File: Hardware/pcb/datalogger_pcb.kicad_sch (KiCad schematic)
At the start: 45 parts, among them J1 Micro_SD_Card_Det2, J2 Switch OUT, SW1 SW_Wuerth_450301014042, U1 DS3231MZ

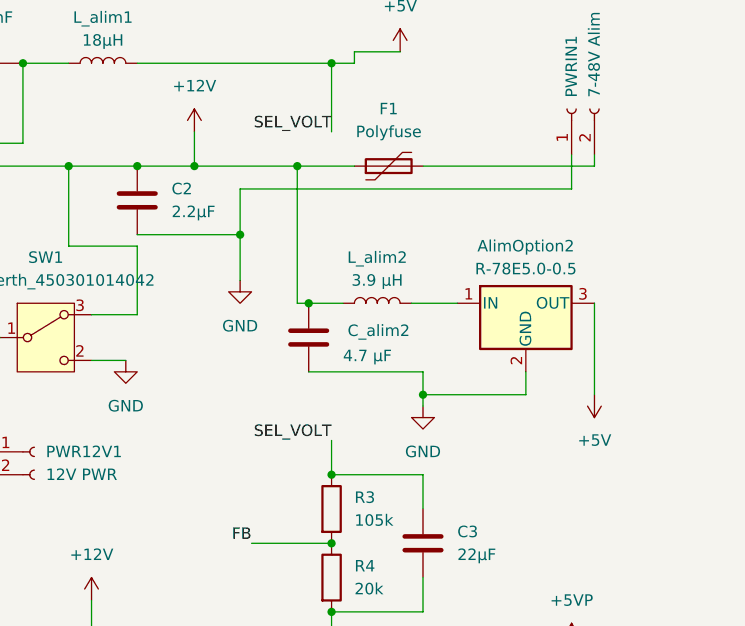
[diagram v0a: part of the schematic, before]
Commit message: Corrected screw diameter error
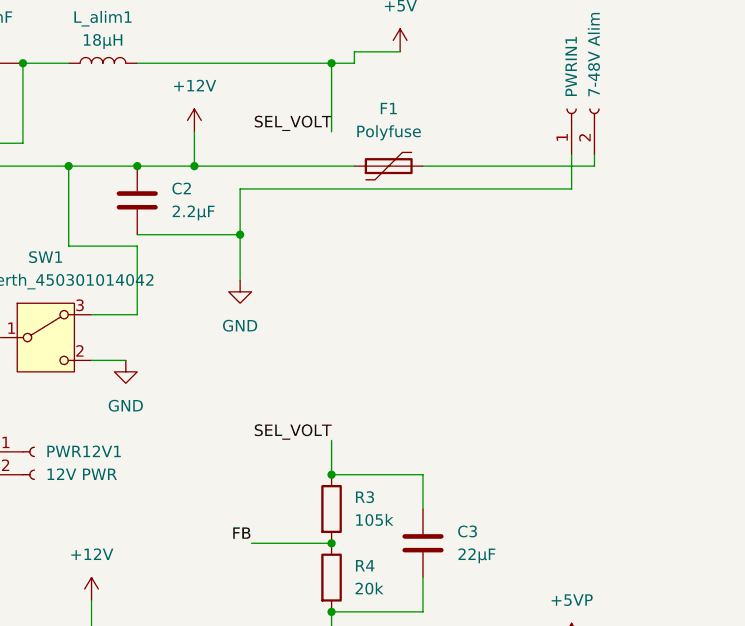
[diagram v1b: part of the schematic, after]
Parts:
- removed AlimOption2: R-78E5.0-0.5, Converter_DCDC:Converter_DCDC_RECOM_R-78E-0.5_THT, symbol Regulator_Switching:R-78E5.0-0.5
- removed C_alim2: 4.7 µF, Capacitor_SMD:C_1812_4532Metric_Pad1.57x3.40mm_HandSolder, symbol Device:C
- removed L_alim2: 3.9 µH, useful:RLS-397, symbol Device:L

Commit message: Added latching shutdown
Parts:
- removed Diodeprotectionalim1: 1N5817, Diode_THT:D_DO-41_SOD81_P10.16mm_Horizontal, symbol Diode:1N5817
- removed R6: 10k, Resistor_SMD:R_0805_2012Metric_Pad1.20x1.40mm_HandSolder, symbol Device:R
- added P_MOSFET1: Si2319CDS, Package_TO_SOT_SMD:SOT-23, symbol Transistor_FET:Si2319CDS
- added R_pullup_int1, R_pullup_shtdwn1: 100k, Resistor_SMD:R_0805_2012Metric_Pad1.20x1.40mm_HandSolder, symbol Device:R
- added U2: SN74LVC2G00DCTR, nand:SSOP-8_2.95x2.8mm_P0.65mm - SN74LVC2G00, symbol SN74LVC2G00DCTR:SN74LVC2G00DCTR
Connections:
- net +5V: now also P_MOSFET1.3 (D), R_pullup_int1.1, R_pullup_shtdwn1.2, U2.8 (VCC)
- net +5VP: now also P_MOSFET1.2 (S)
- net GND: now also U2.4 (GND)
- net at A1.20 (GPIO15), GPIO14-1.3 (Pin_3): no longer U1.3 (~{INT}/SQW)
- new net: P_MOSFET1.1 (G), U2.6 (2B), U2.7 (1Y)
- new net: U2.2 (1B), U2.3 (2Y)
- new net RTC_INT: R_pullup_int1.2, U1.3 (~{INT}/SQW), U2.1 (1A)
- new net SHTDWN_CTRL: R_pullup_shtdwn1.1, U2.5 (2A)
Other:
- moved on the sheet: 5VPOUT1

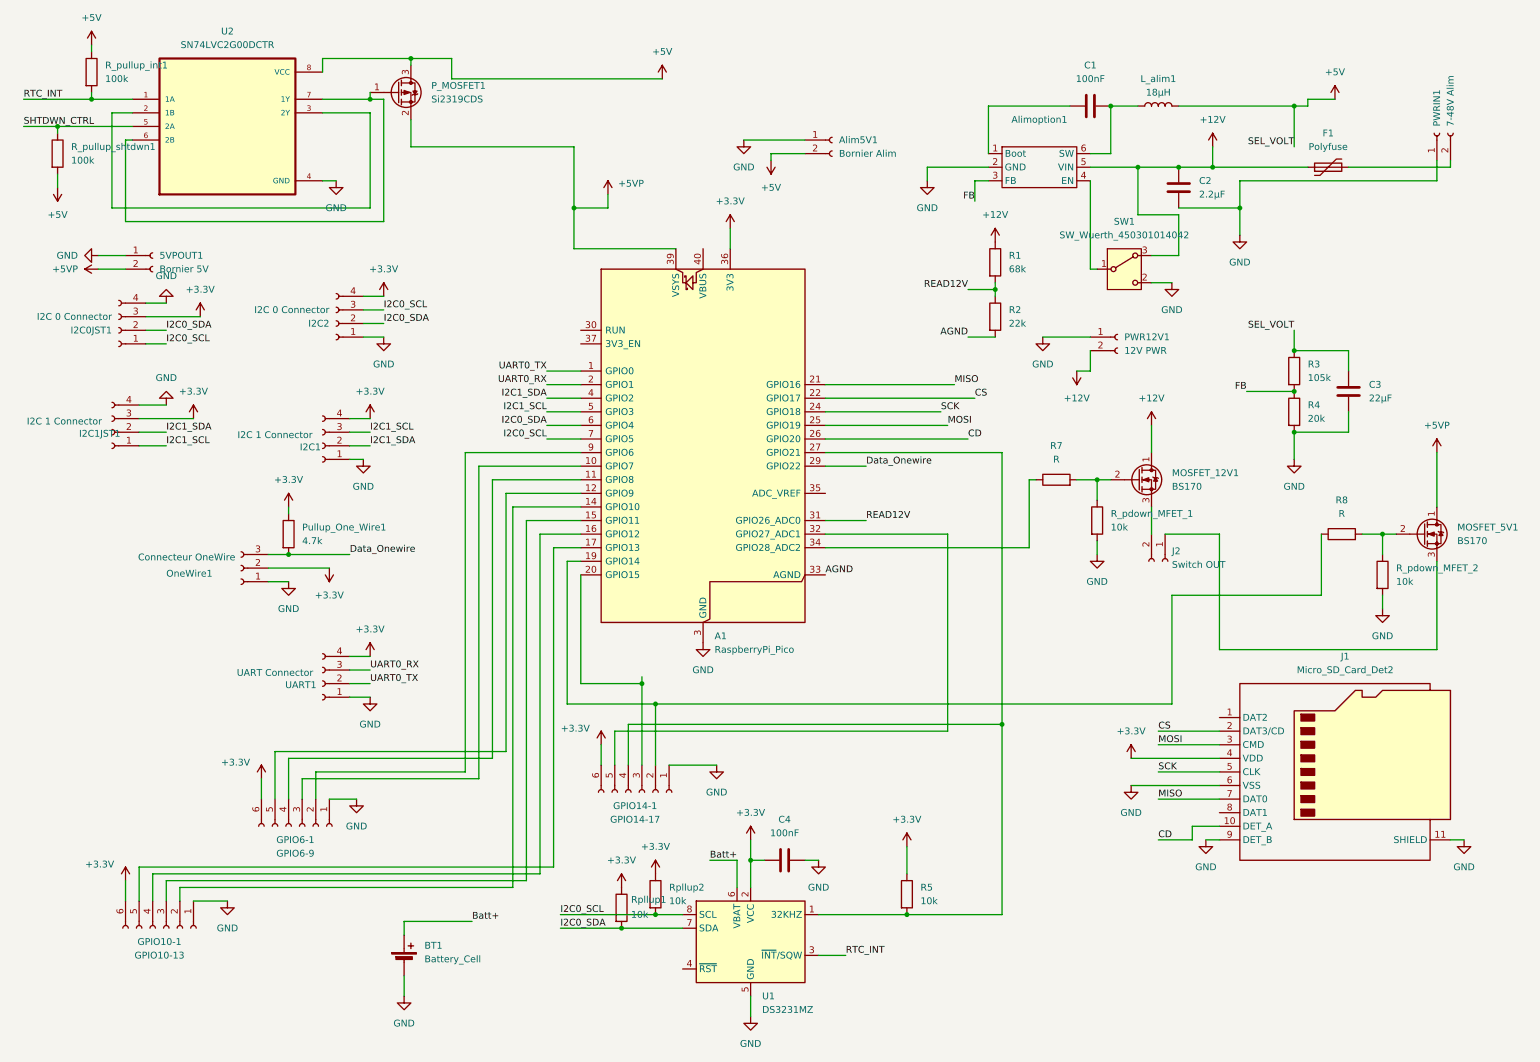
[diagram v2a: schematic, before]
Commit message: Added PAR sensor PCB
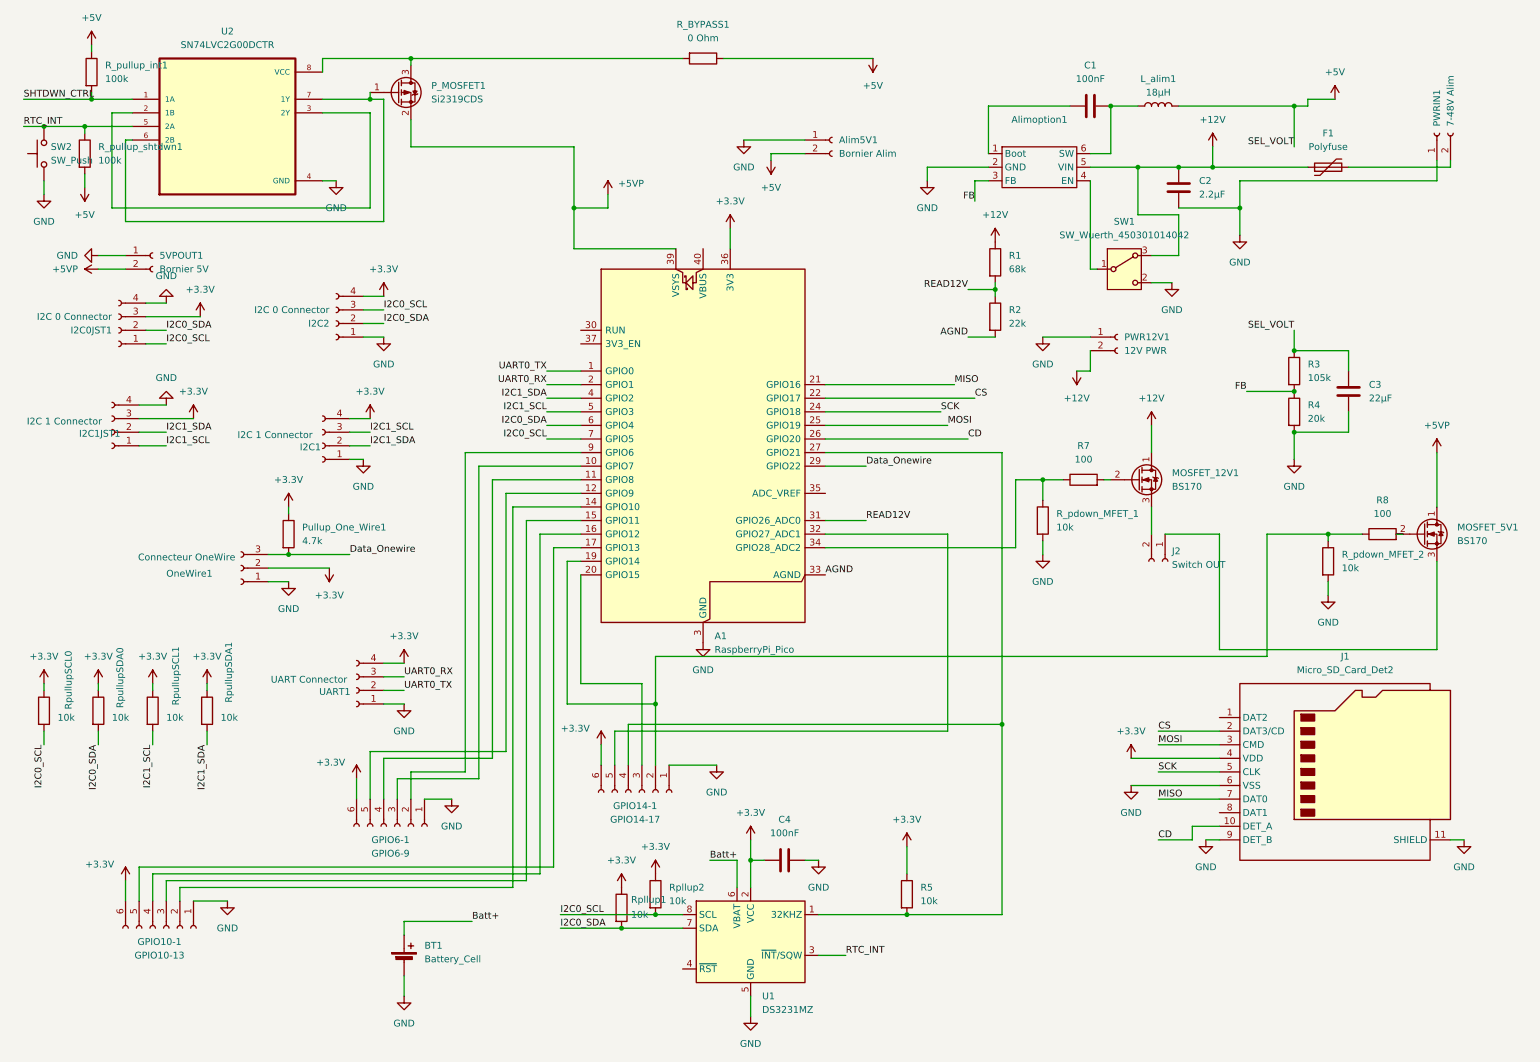
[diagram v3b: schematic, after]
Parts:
- added R_BYPASS1: 0 Ohm, Resistor_THT:R_Axial_DIN0204_L3.6mm_D1.6mm_P5.08mm_Vertical, symbol Device:R
- added RpullupSCL0, RpullupSCL1, RpullupSDA0, RpullupSDA1: 10k, Resistor_THT:R_Axial_DIN0204_L3.6mm_D1.6mm_P5.08mm_Vertical, symbol Device:R
- added SW2: SW_Push, Button_Switch_THT:SW_PUSH_6mm_H4.3mm, symbol Switch:SW_Push
- R7, R8: value R -> 100
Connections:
- net +3.3V: now also RpullupSCL0.1, RpullupSCL1.1, RpullupSDA0.1, RpullupSDA1.1
- net +5V: now also R_BYPASS1.1; no longer P_MOSFET1.3 (D), U2.8 (VCC)
- net GND: now also SW2.1
- net I2C0_SCL: now also RpullupSCL0.2
- net I2C0_SDA: now also RpullupSDA0.2
- net I2C1_SCL: now also RpullupSCL1.2
- net I2C1_SDA: now also RpullupSDA1.2
- net RTC_INT: now also R_pullup_shtdwn1.1, U2.5 (2A), SW2.2; no longer R_pullup_int1.2, U2.1 (1A)
- net SHTDWN_CTRL: now also R_pullup_int1.2, U2.1 (1A); no longer R_pullup_shtdwn1.1, U2.5 (2A)
- net at A1.34 (GPIO28_ADC2), R7.1: now also R_pdown_MFET_1.1
- net at MOSFET_12V1.2 (G), R7.2: no longer R_pdown_MFET_1.1
- net at A1.19 (GPIO14), GPIO14-1.2 (Pin_2), R8.1: now also R_pdown_MFET_2.1
- net at MOSFET_5V1.2 (G), R8.2: no longer R_pdown_MFET_2.1
- new net: P_MOSFET1.3 (D), R_BYPASS1.2, U2.8 (VCC)
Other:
- moved on the sheet: GPIO6-1, R7, R8, R_pdown_MFET_1, R_pdown_MFET_2, R_pullup_shtdwn1, UART1
